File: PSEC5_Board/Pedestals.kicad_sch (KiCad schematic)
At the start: 48 parts, among them J11 Conn_Coaxial, J2 Conn_Coaxial, J3 Conn_Coaxial, J4 Conn_Coaxial, J5 Conn_Coaxial, J6 Conn_Coaxial, J7 Conn_Coaxial, J8 Conn_Coaxial

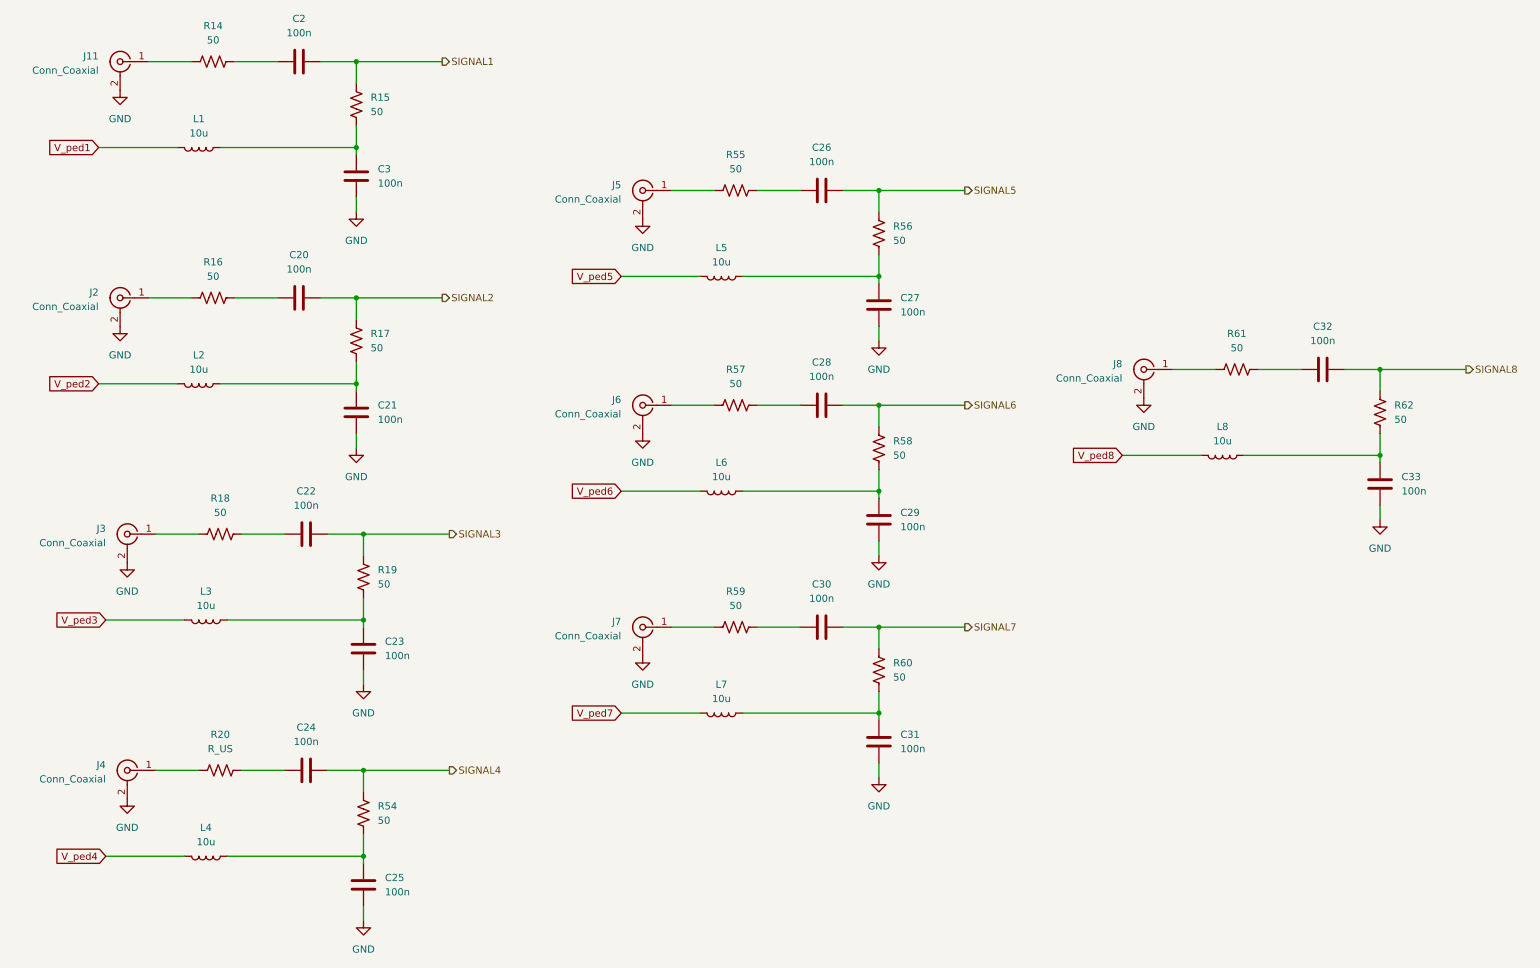
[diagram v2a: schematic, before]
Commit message: DUT v4 Push
Addressed the issues discussed in last week's meeting, cleared ERC errors, still any warnings with Solder Mask.
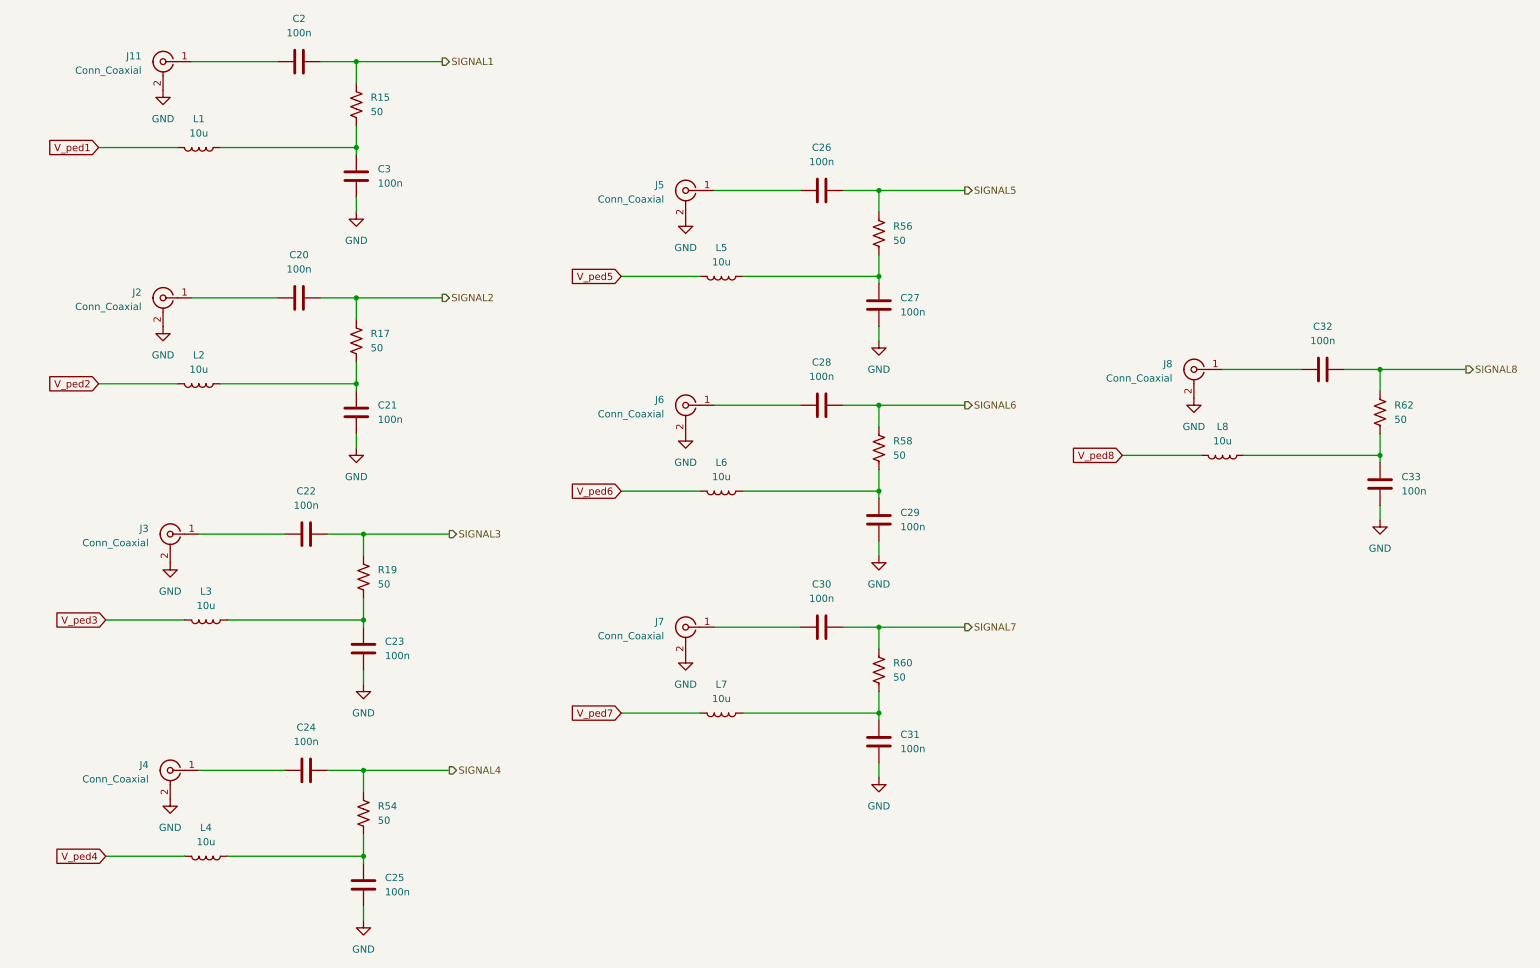
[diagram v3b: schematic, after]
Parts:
- removed R14, R16, R18, R55, R57, R59, R61: 50, Resistor_SMD:R_0603_1608Metric, symbol Device:R_US
- removed R20: R_US, Resistor_SMD:R_0603_1608Metric, symbol Device:R_US
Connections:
- net at J3.1 (In): now also C22.2
- net at C30.2: now also J7.1 (In)
- net at C24.2: now also J4.1 (In)
- net at C2.2: now also J11.1 (In)
- net at C26.2: now also J5.1 (In)
- net at C32.2: now also J8.1 (In)
- net at J2.1 (In): now also C20.2
- net at C28.2: now also J6.1 (In)
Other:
- moved on the sheet: J11, J2, J3, J4, J5, J6, J7, J8

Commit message: Merge Richmond's production board from JoeModifications into same branch as other boards
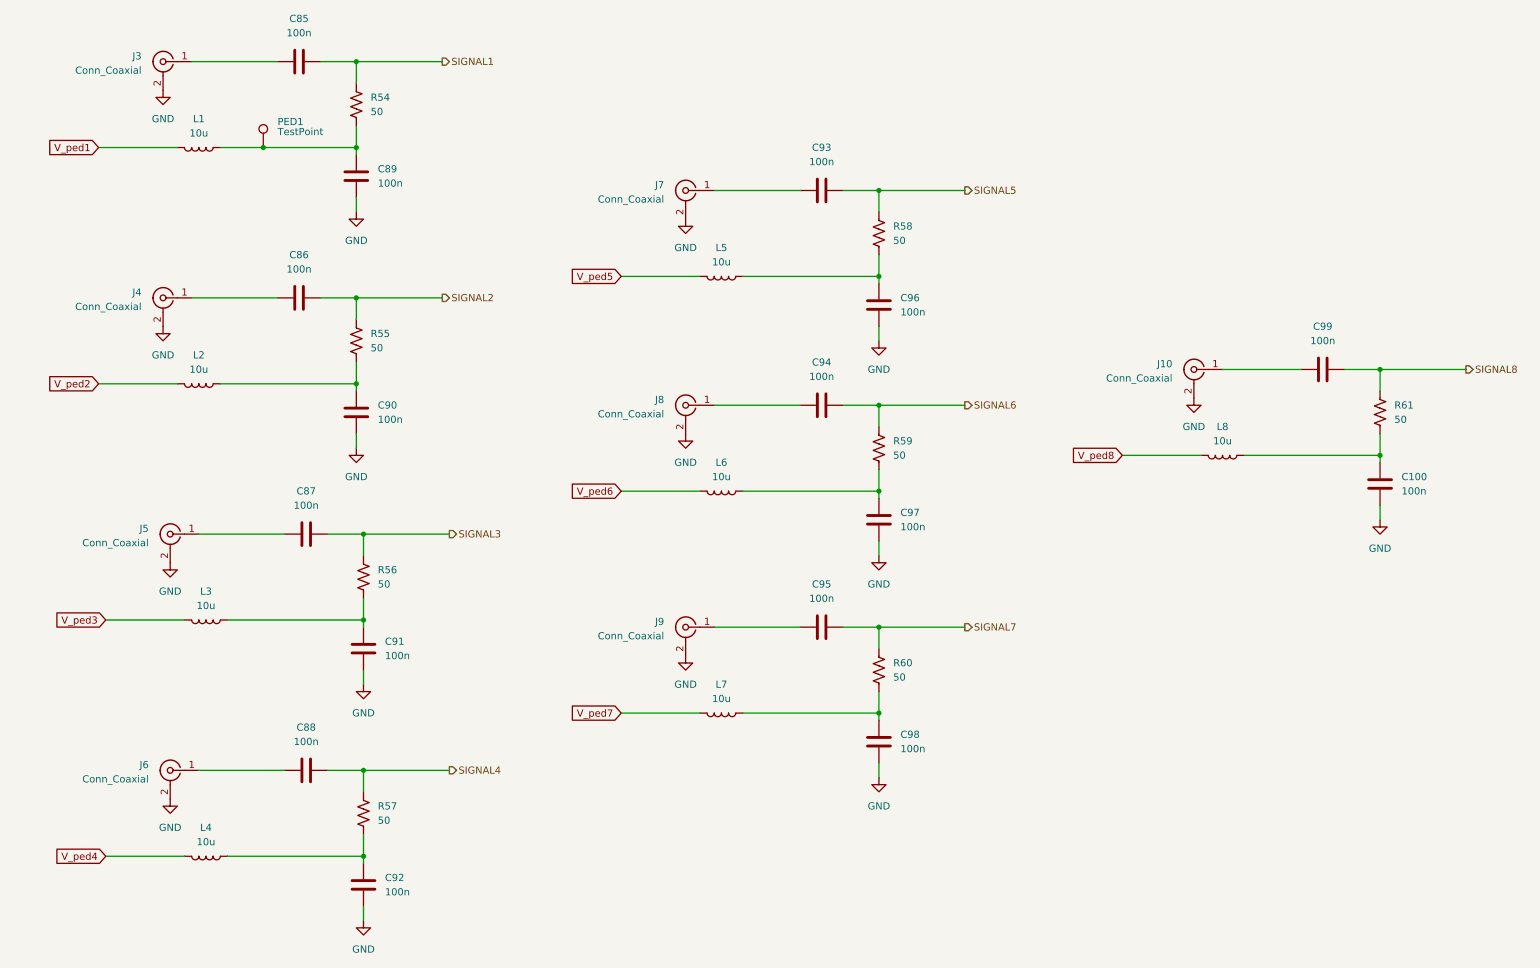
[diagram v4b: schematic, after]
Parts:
- added PED1: TestPoint, TestPoint:TestPoint_THTPad_1.0x1.0mm_Drill0.5mm, symbol Connector:TestPoint
- renumbered C33 to C100, C2 to C85, C20 to C86, C22 to C87, C24 to C88, C3 to C89, C21 to C90, C23 to C91, C25 to C92, C26 to C93, C28 to C94, C30 to C95, C27 to C96, C29 to C97, C31 to C98, C32 to C99, J8 to J10, J11 to J3, J2 to J4, J3 to J5, J4 to J6, J5 to J7, J6 to J8, J7 to J9, R15 to R54, R17 to R55, R19 to R56, R54 to R57, R56 to R58, R58 to R59, R62 to R61
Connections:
- net at C89.1, L1.1, R54.1: now also PED1.1
